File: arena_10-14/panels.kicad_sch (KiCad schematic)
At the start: 0 parts

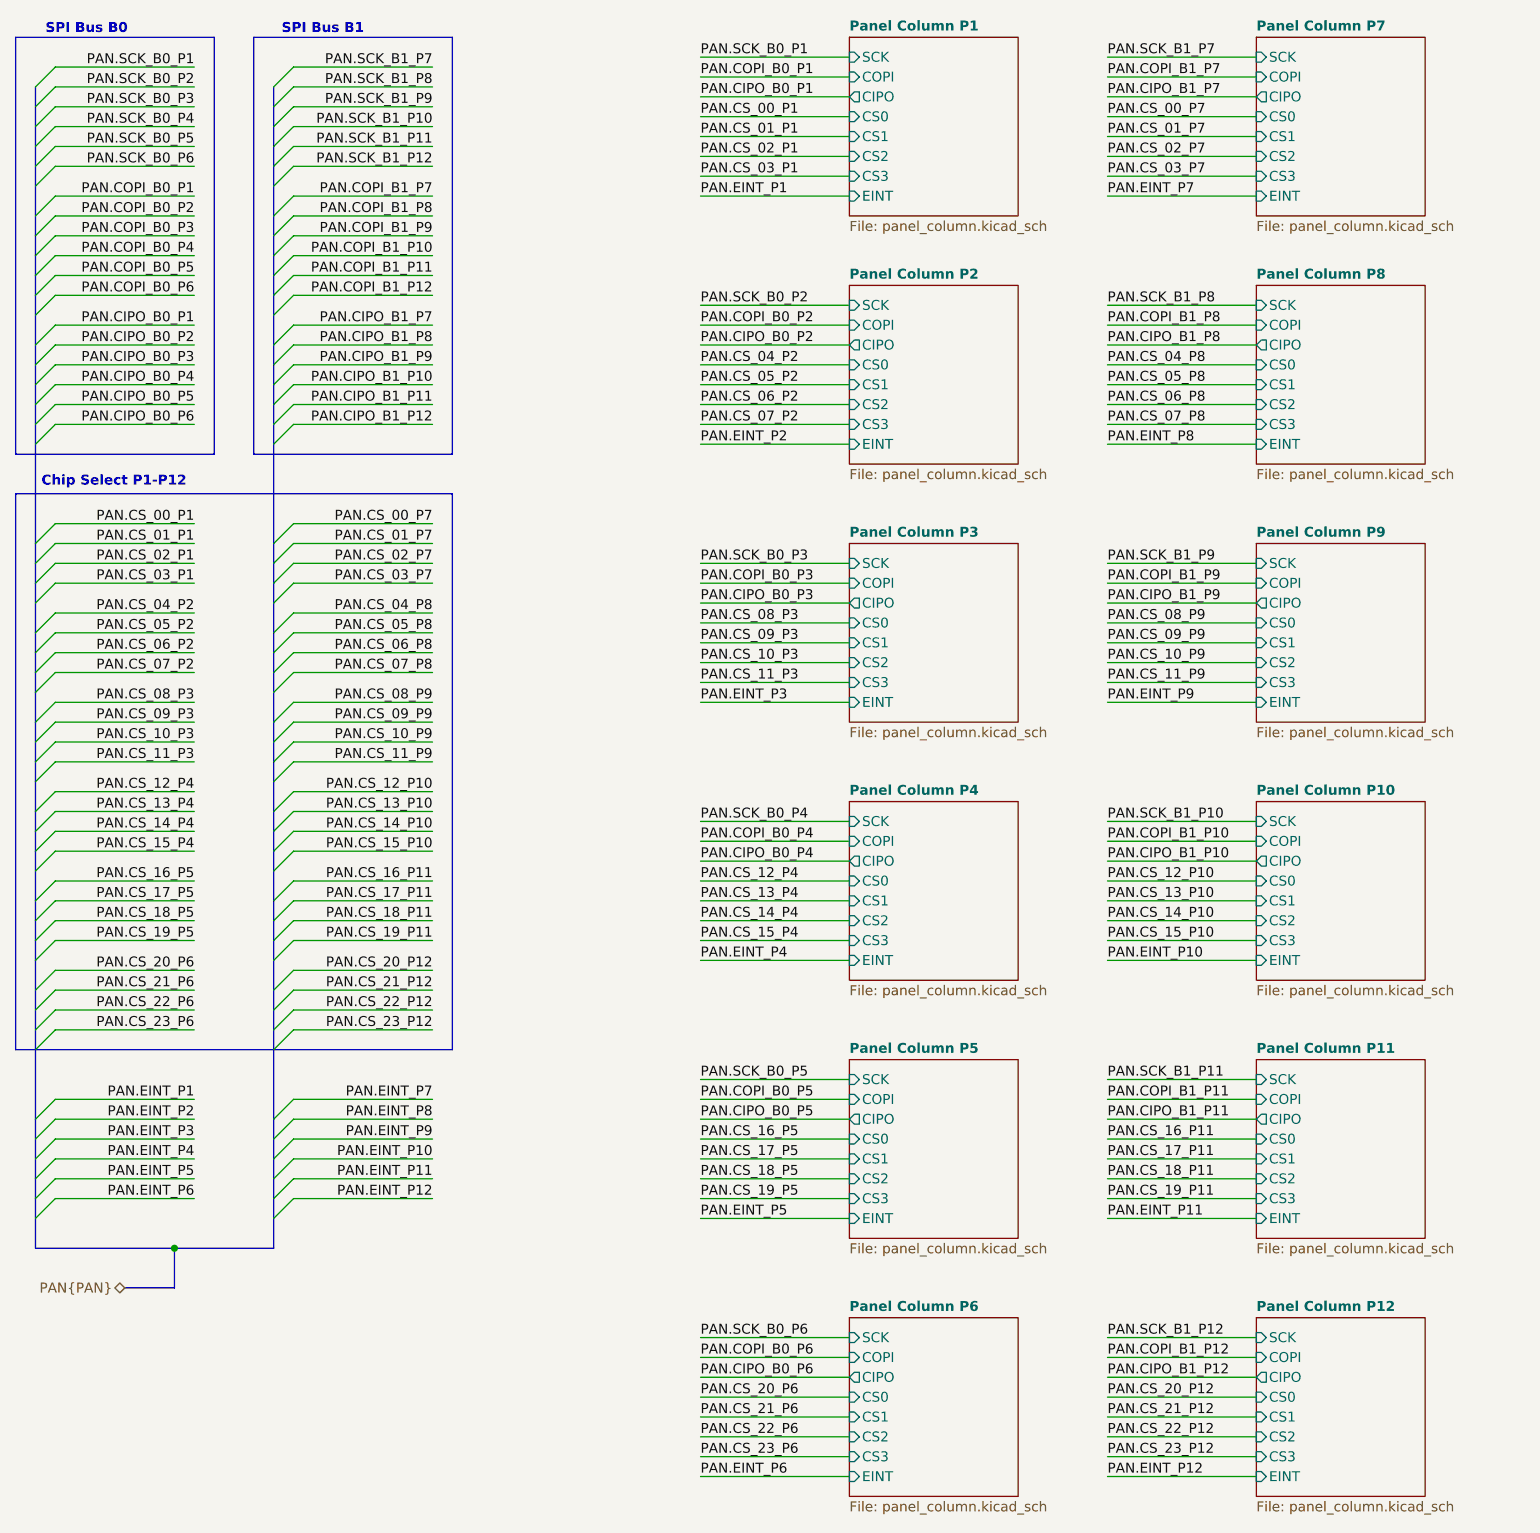
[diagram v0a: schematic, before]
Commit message: feat: reduce 10-14 arena to 10 panel columns and add digital IO channels
Schematic
- Remove panel columns P11 and P12; the Panels sheet now holds P1..P10.
- Re-split the SPI banks for 10 panels: B0 serves P1-P5, B1 serves
  P6-P10 (CIPO enables, SCK/COPI/EINT fan-out).
- Re-pair the chip selects: CS_00..19 each fan out to (Pn, Pn+5), and
  the CS_20..23 fan-out sheets are gone.
- The shared SCK/COPI/EINT dual buffers now drive P1/P2, P3/P4, P6/P7
  and P8/P9. The buffers for P5 and P10 each drive a single panel.
- Move the Teensy digital IO channel (SN74LVC1T45 level shifter and BNC
  connector) into a new DIO.kicad_sch sub-sheet and instance it four
  times (Digital IO 01..04).

PCB
- Update from the schematic: the P11/P12 columns and their parts are
  removed (623 -> 547 footprints, no P11/P12 nets left). The freed
  references U78-U80, J25, J26 and J34 now belong to the digital IO
  channels.
- Most of the old 12-panel routing is removed (4471 -> 1393
  tracks/vias).

Placement scripts (assets/placement/)
- 01, 02: end each footprint block at its own closing paren. The last
  footprint in the file used to extend to the end of the file, so 02
  added an angle to every via and KiCad refused to open the board
  ("Expecting ')'").
- 03: replicate to P1..P10 only and ignore CIPO-enable sheets beyond
  P10. Read the B0/B1 bank of the PAN and TNY nets from the board
  instead of hardcoding P1-P6 / P7-P12. Same footprint-block fix.
- 05: read each CS group's panel pair and midpoint anchor from the
  fan-out sheet names instead of hardcoding P(4+j), and stop if a
  midpoint is not a populated connector. Same footprint-block fix (05
  rewrites footprints, so it could corrupt vias the same way 02 did).

Known gaps, to follow up
- 05 stops on the new CS pairing: the P1/P6 midpoint is P3.5, so an
  anchor for each group still has to be chosen.
- 02 and 03 still pair the shared buffers as P1/P2, P3/P4, P5/P6,
  P7/P8, P9/P10, anchored on the even connector. With the new B1
  p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
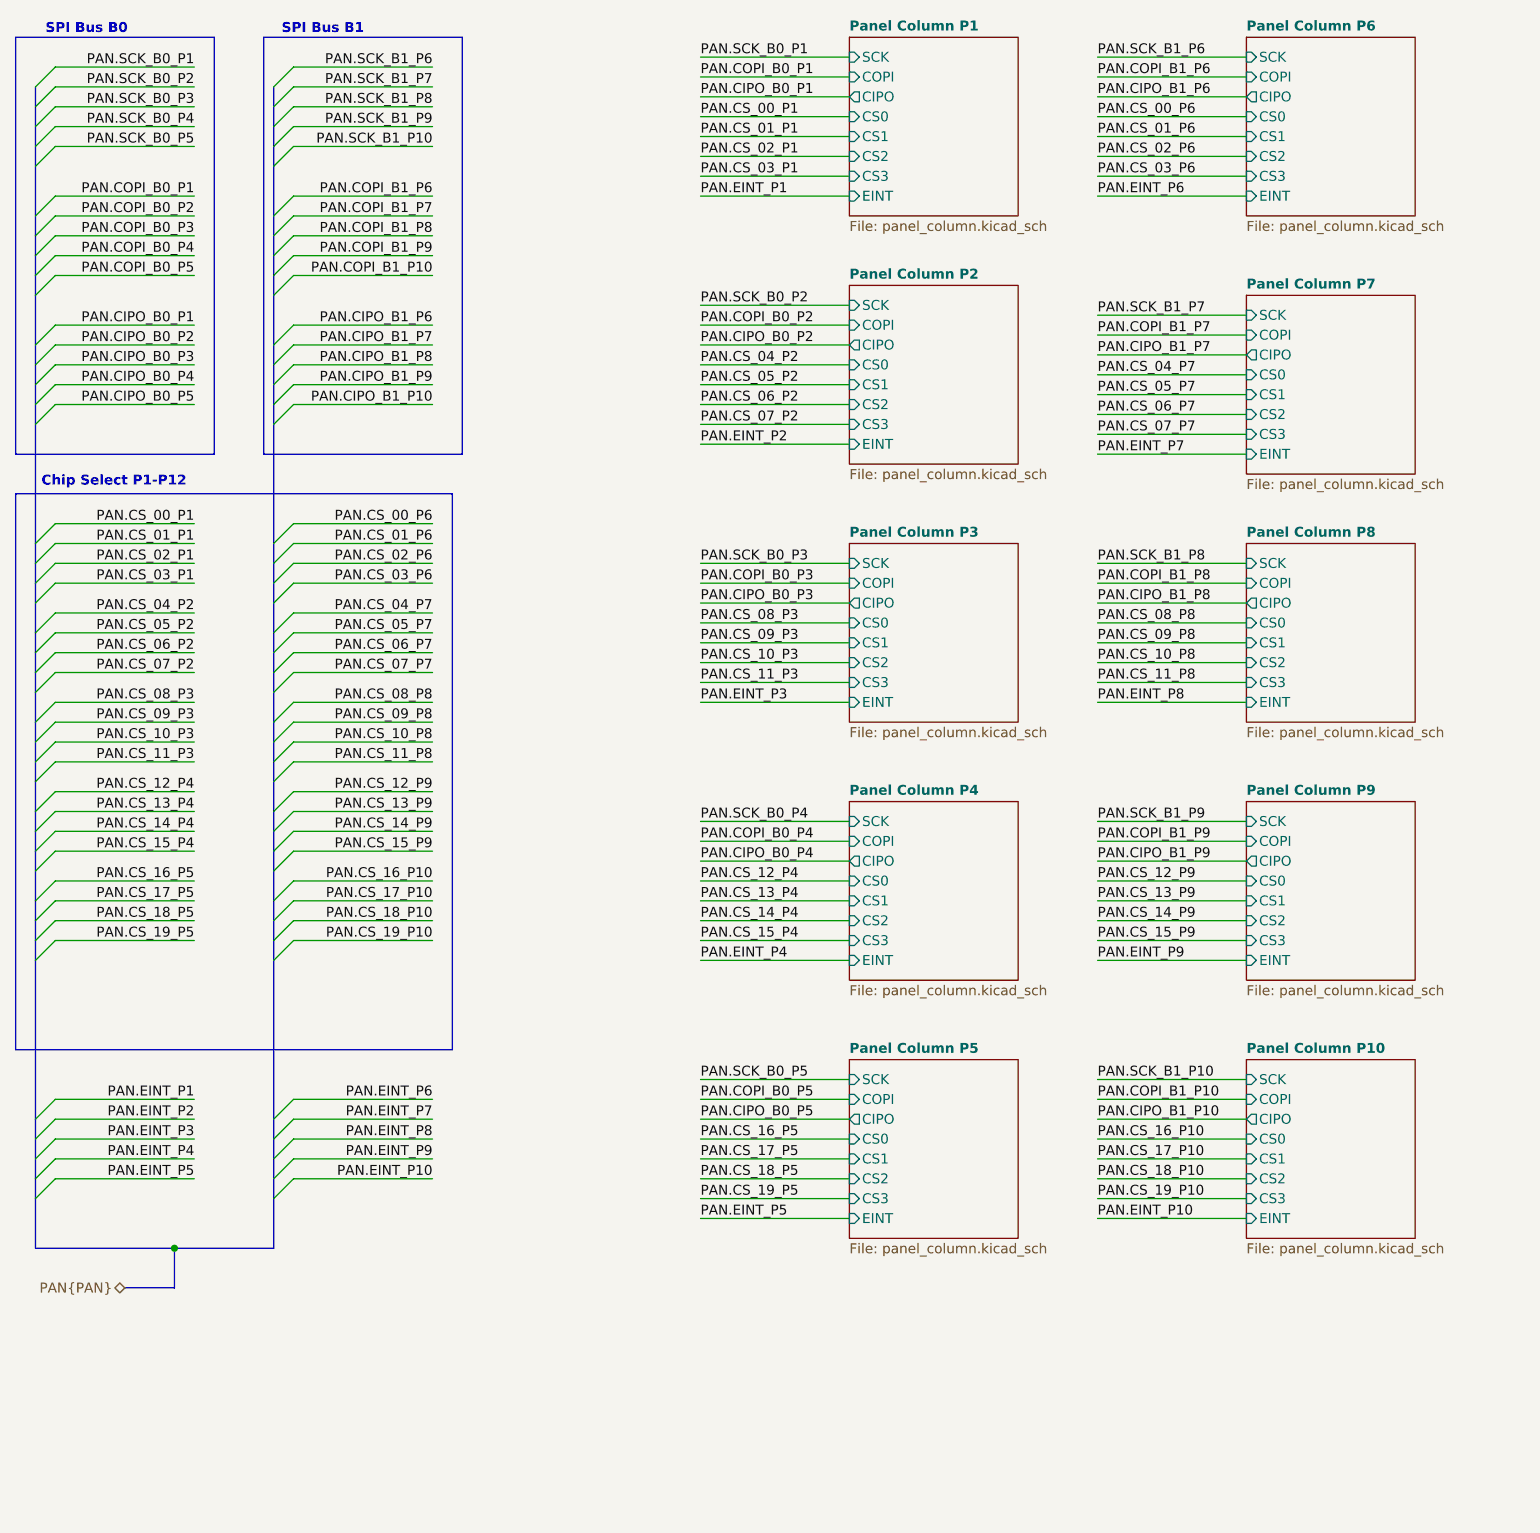
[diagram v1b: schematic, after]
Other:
- removed sheet Panel Column P11
- removed sheet Panel Column P12
